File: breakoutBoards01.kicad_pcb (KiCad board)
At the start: 2 copper layers, 45.7 x 45.7 mm, 5 parts, among them J1 CONN_25X1, J2 CONN_25X1, J3 CONN_25X1, J4 CONN_25X1, U1 100PIN

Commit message: better layout
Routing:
- net N-0000095: track 20.0 -> 0.00 mm
- net N-0000045: track 19.4 -> 0.00 mm
- net N-0000093: track 19.2 -> 0.00 mm
- net N-0000052: track 19.1 -> 0.00 mm
- net N-0000016: track 18.7 -> 0.00 mm
- net N-0000082: track 18.6 -> 0.00 mm
- net N-0000092: track 18.4 -> 0.00 mm
- net N-0000090: track 17.8 -> 0.00 mm
- net N-0000043: track 17.7 -> 0.00 mm
- net N-0000018: track 17.7 -> 0.00 mm
- net N-0000080: track 17.7 -> 0.00 mm
- net N-0000078: track 17.2 -> 0.00 mm
- net N-0000041: track 17.1 -> 0.00 mm
- net N-0000020: track 17.1 -> 0.00 mm
- net N-0000050: track 16.9 -> 0.00 mm
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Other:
- board text added: "0.5mm pitch QFP"
- board text removed: "TQFP48 TQFP64 TQFP80 TQFP100 0.5mm pitch"

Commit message: rename
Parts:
- U1: footprint TQFP48-100 -> QFP0.5mm
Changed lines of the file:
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@@
     )
   )
-  (module TQFP48-100 (layer F.Cu)
+  (module QFP0.5mm (layer F.Cu)
     (at 122.86 122.86)
     (clearance 0.2)

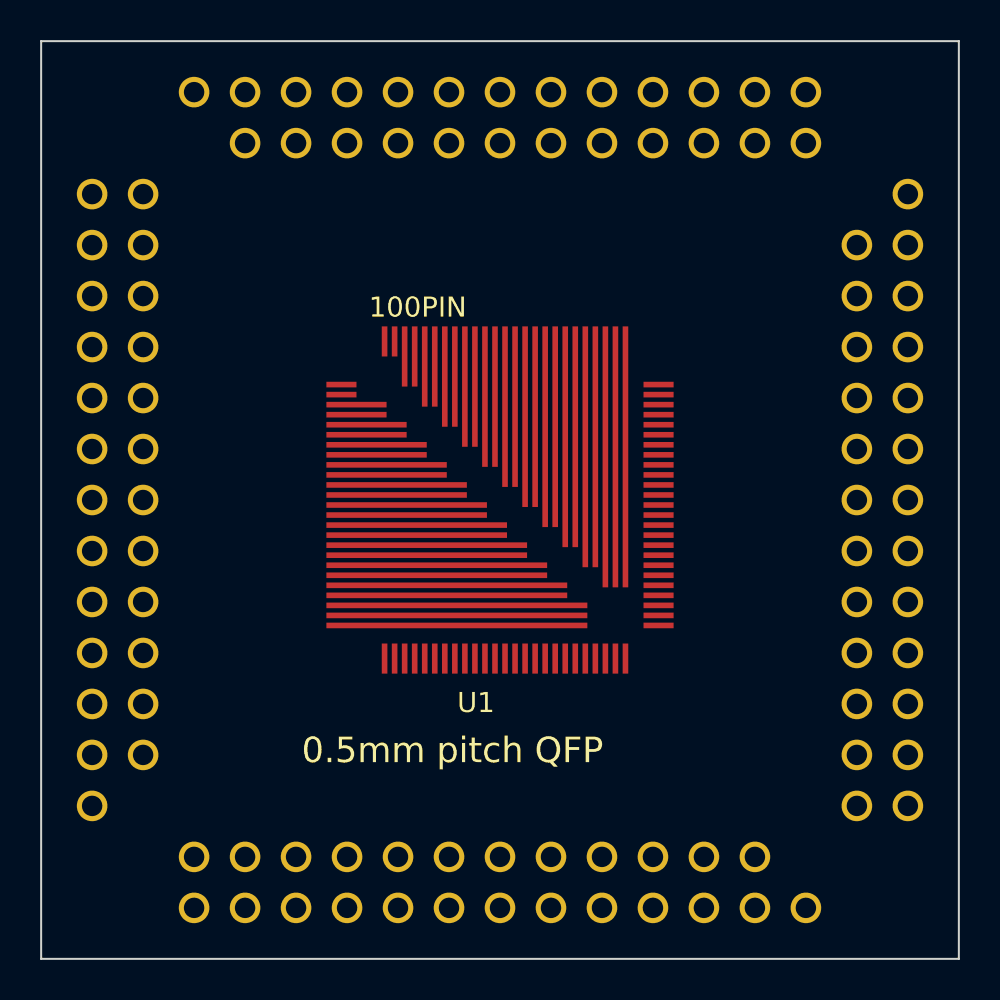
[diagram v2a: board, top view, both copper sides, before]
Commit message: mounting holes and wireup
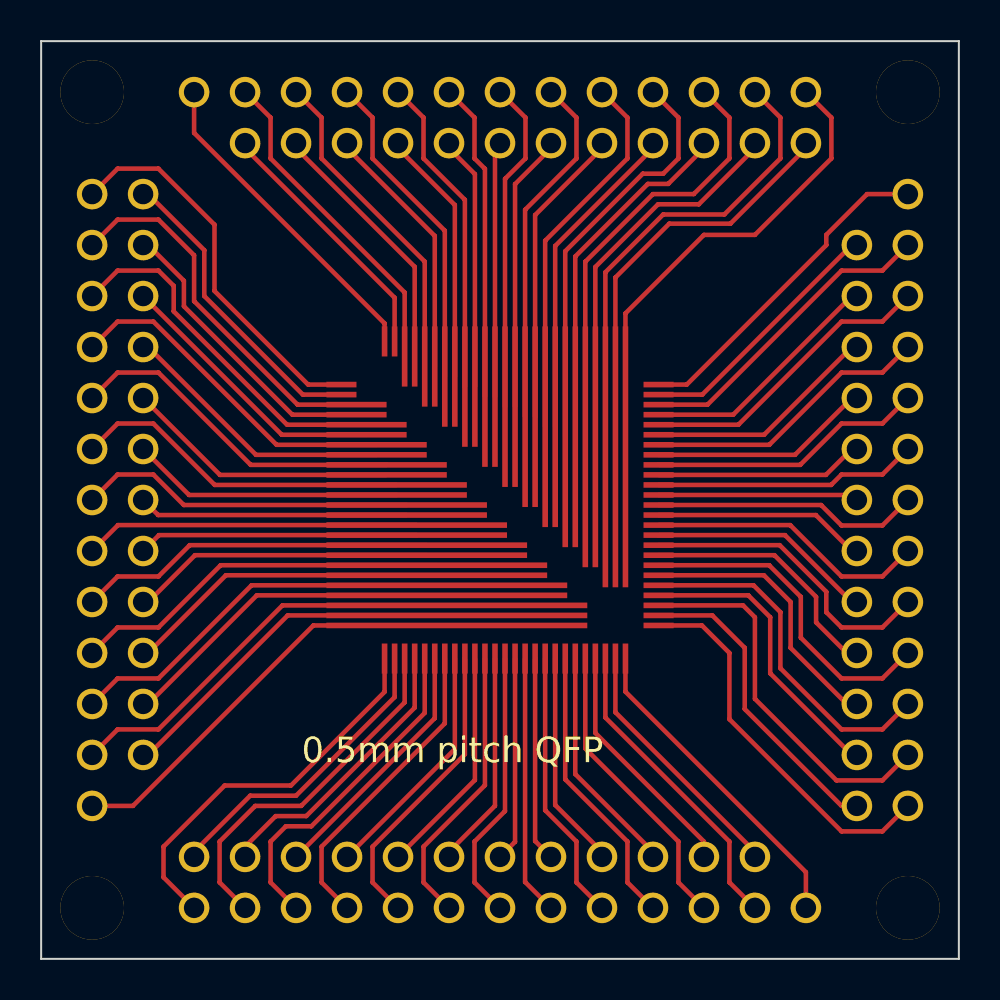
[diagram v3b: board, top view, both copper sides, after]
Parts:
- added M1: Mounting Hole, MOUNTING_HOLE_0.125in, F.Cu at (143.2, 143.2)
- added M2: Mounting Hole, MOUNTING_HOLE_0.125in, F.Cu at (143.2, 102.5)
- added M3: Mounting Hole, MOUNTING_HOLE_0.125in, F.Cu at (102.5, 102.5)
- added M4: Mounting Hole, MOUNTING_HOLE_0.125in, F.Cu at (102.5, 143.2)
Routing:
- net N-0000016: track 0.00 -> 24.4 mm
- net N-0000018: track 0.00 -> 24.1 mm
- net N-0000020: track 0.00 -> 22.4 mm
- net N-0000096: track 0.00 -> 21.9 mm
- net N-0000017: track 0.00 -> 21.3 mm
- net N-0000098: track 0.00 -> 21.3 mm
- net N-0000022: track 0.00 -> 20.6 mm
- net N-00000100: track 0.00 -> 20.1 mm
- net N-0000019: track 0.00 -> 19.6 mm
- net N-0000095: track 0.00 -> 19.5 mm
- net N-0000045: track 0.00 -> 19.3 mm
- net N-0000052: track 0.00 -> 19.1 mm
- net N-0000066: track 0.00 -> 19.0 mm
- net N-0000043: track 0.00 -> 18.9 mm
- net N-0000024: track 0.00 -> 18.9 mm
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
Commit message: version numbers
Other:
- board text added: "https://github.com/joeferner/breakoutBoards"
- board text added: "v1"
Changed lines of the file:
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@@
     (links 100)
     (no_connects 0)
-    (area 96.116623 99.1964 149.933377 146.5236)
+    (area 94.864178 99.1964 150.555822 147.8086)
     (thickness 1.6)
-    (drawings 5)
+    (drawings 7)
     (tracks 386)
     (zones 0)
@@
     (pad_to_mask_clearance 0)
     (aux_axis_origin 100 100)
-    (visible_elements FFFFFFBF)
+    (visible_elements FFFFFF3F)
     (pcbplotparams
       (layerselection 3178497)
@@
     )
   )
+  (gr_text v1 (at 122.174 124.714) (layer B.SilkS)
+    (effects (font (size 1.5 1.5) (thickness 0.3)) (justify mirror))
+  )
+  (gr_text https://github.com/joeferner/breakoutBoards (at 123.952 122.174) (layer B.SilkS)
+    (effects (font (size 1 1) (thickness 0.15)) (justify mirror))
+  )
   (gr_text "0.5mm pitch QFP" (at 112.9794 135.3314) (layer F.SilkS)
